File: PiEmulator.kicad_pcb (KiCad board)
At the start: 2 copper layers, 15 parts, among them J3 USB_C_Receptacle_USB2.0, U1 ADA3708, U3 BQ24090DGQ

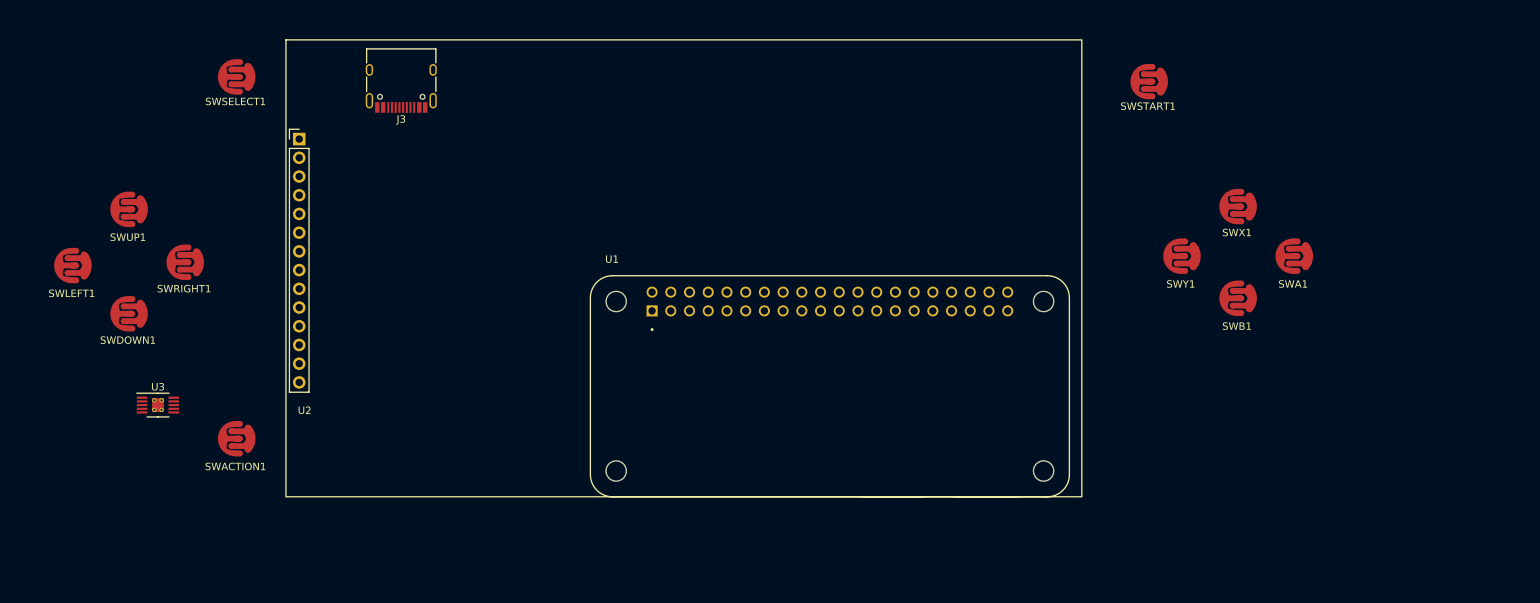
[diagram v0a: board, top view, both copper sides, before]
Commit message: swapped buttons
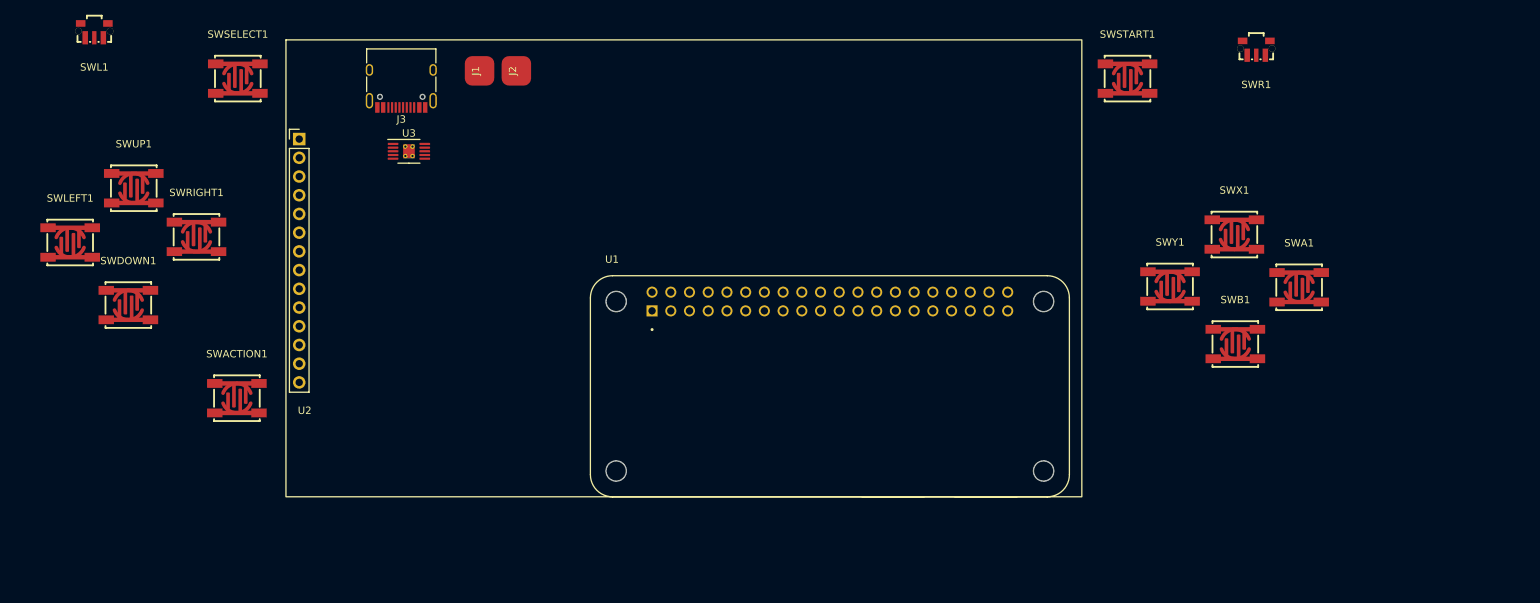
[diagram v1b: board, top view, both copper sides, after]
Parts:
- added J1: Conn_01x01, Connector_Wago:SolderWirePad_4x4mm, F.Cu at (99.8, 61.8)
- added J2: Conn_01x01, Connector_Wire:Solder_Pad_4x4mm, F.Cu at (104.8, 61.8)
- added SWL1: TSA020A3418A, easyeda2kicad:SW-SMD_TSA020XXXXXX, F.Cu at (47.5, 56.4)
- added SWR1: TSA020A3418A, easyeda2kicad:SW-SMD_TSA020XXXXXX, F.Cu at (205.2, 58.8)
- SWA1, SWACTION1, SWB1, SWDOWN1, SWLEFT1, SWRIGHT1, SWSELECT1, SWSTART1, SWUP1, SWX1, SWY1: footprint Button_Switch_SMD:PCB-Button -> easyeda2kicad:SW-SMD_4P-L6.2-W6.2-P4.00-LS7.0
- moved U3 48.4 mm to (90.2, 72.8)
- moved SWACTION1 8.03 mm to (66.8, 106.3)
- moved SWRIGHT1 6.22 mm to (61.4, 84.4)
- moved SWLEFT1 5.67 mm to (44.2, 85.1)
- moved SWUP1 5.47 mm to (52.9, 77.8)
- moved SWSTART1 4.06 mm to (187.7, 62.9)
- moved SWDOWN1 3.72 mm to (52.1, 93.6)
- moved SWB1 3.68 mm to (202.3, 98.9)
- moved SWSELECT1 2.33 mm to (67.0, 62.9)
- moved SWY1 2.15 mm to (193.5, 91.1)
- moved SWA1 1.87 mm to (211.0, 91.2)
- moved SWX1 1.31 mm to (202.2, 84.1)
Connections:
- U3 pad 10: unconnected-(U3-OUT-Pad10) -> Net-(J1-Pin_1)
- U3 pad 5: unconnected-(U3-~{PG}-Pad5) -> Net-(D1-K)
- U3 pad 8: unconnected-(U3-~{CHG}-Pad8) -> Net-(D2-K)
- U3 pad 9: unconnected-(U3-TS-Pad9) -> Net-(U3-TS)

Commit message: routed
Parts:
- added D1: BLUE, LED_SMD:LED_0402_1005Metric, F.Cu at (181.9, 73.5)
- added D2: RED, LED_SMD:LED_0402_1005Metric, F.Cu at (181.9, 75.4)
- added R1: 540, Resistor_SMD:R_0603_1608Metric, B.Cu at (91.2, 70.5)
- added R2: 2K, Resistor_SMD:R_0603_1608Metric, B.Cu at (91.8, 73.2)
- added R3: 1K5, Resistor_SMD:R_0402_1005Metric, F.Cu at (184.0, 73.5)
- added R4: 1K5, Resistor_SMD:R_0402_1005Metric, F.Cu at (184.0, 75.4)
- added R5: 10K, Resistor_SMD:R_0402_1005Metric, B.Cu at (80.9, 72.5)
- J1, J2, J3, U3: moved to B.Cu
- moved J1 11.1 mm to (105.4, 71.4)
- moved J2 10.5 mm to (100.1, 71.2)
- moved SWACTION1 7.15 mm to (62.0, 111.5)
- moved SWX1 7.09 mm to (201.6, 77.0)
- moved SWL1 5.52 mm to (47.3, 61.9)
- moved SWRIGHT1 4.94 mm to (59.6, 89.0)
- moved U3 4.83 mm to (85.5, 71.6), turned to 180 degrees
- moved SWY1 4.39 mm to (189.6, 89.0)
- moved SWR1 4.31 mm to (202.3, 62.0)
- moved SWUP1 4.23 mm to (52.6, 82.0)
- moved SWLEFT1 4.11 mm to (45.6, 89.0)
- moved J3 3.58 mm to (85.6, 63.2), turned to 0 degrees
- moved SWA1 3.44 mm to (213.6, 89.0)
- moved SWSELECT1 3.42 mm to (63.7, 63.9)
- moved U1 3.42 mm to (144.0, 105.6)
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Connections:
- J1 pad 1: Net-(J1-Pin_1) -> +BATT
- U1 pad 12: /A -> /X
- U1 pad 13: unconnected-(U1-GPIO27_GEN2-Pad13) -> /Right
- U1 pad 14: unconnected-(U1-GND_4-Pad14) -> GND
- U1 pad 2: unconnected-(U1-5V_1-Pad2) -> +BATT
- U1 pad 20: unconnected-(U1-GND_5-Pad20) -> GND
- U1 pad 25: unconnected-(U1-GND_2-Pad25) -> GND
- U1 pad 29: /Right -> /Left
- U1 pad 3: /RB -> /Action
- U1 pad 30: /B -> GND
- U1 pad 31: /Left -> /Down
- U1 pad 32: /X -> /A
- U1 pad 33: /Down -> /Up
- U1 pad 34: unconnected-(U1-GND_7-Pad34) -> GND
- U1 pad 35: /Up -> /B
- U1 pad 39: unconnected-(U1-GND_3-Pad39) -> GND
- U1 pad 4: +5V -> +BATT
- U1 pad 40: /Action -> /RB
- U1 pad 9: unconnected-(U1-GND_1-Pad9) -> GND
- U2 pad 1: +5V -> +BATT
- U2 pad 8: +5V -> +BATT
- U3 pad 10: Net-(J1-Pin_1) -> +BATT
- U3 pad 7: unconnected-(U3-ISET2-Pad7) -> GND
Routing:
- net +BATT: track 0.00 -> 188.5 mm, vias 0 -> 1
- net /Up: track 0.00 -> 163.7 mm
- net /Left: track 0.00 -> 123.7 mm
- net /Down: track 0.00 -> 115.5 mm
- net Net-(D2-K): track 0.00 -> 115.3 mm, vias 0 -> 1
- net /Select: track 0.00 -> 110.1 mm, vias 0 -> 1
- net Net-(D1-K): track 0.00 -> 106.4 mm, vias 0 -> 1
- net /LB: track 0.00 -> 97.9 mm
- net /Right: track 0.00 -> 91.3 mm
- net /CLK: track 0.00 -> 87.8 mm, vias 0 -> 1
- net /CS: track 0.00 -> 82.3 mm, vias 0 -> 1
- net /MISO: track 0.00 -> 80.4 mm, vias 0 -> 1
- net /RESET: track 0.00 -> 78.7 mm, vias 0 -> 1
- net /MOSI: track 0.00 -> 77.9 mm, vias 0 -> 1
- net /Action: track 0.00 -> 73.0 mm, vias 0 -> 1
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- added copper zone on B.Cu, net GND
- added copper zone on F.Cu, net GND
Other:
- board outline added: 180 x 60 mm

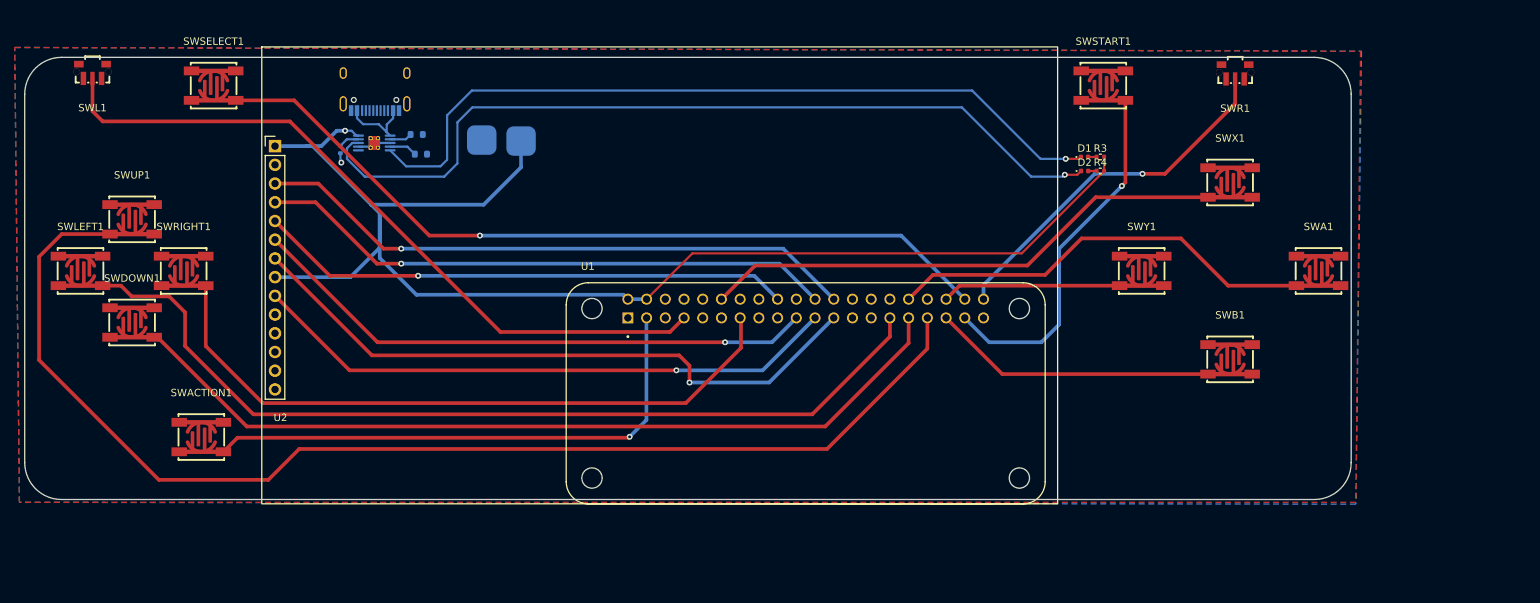
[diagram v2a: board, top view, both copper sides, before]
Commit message: silkscreen + minor fixes
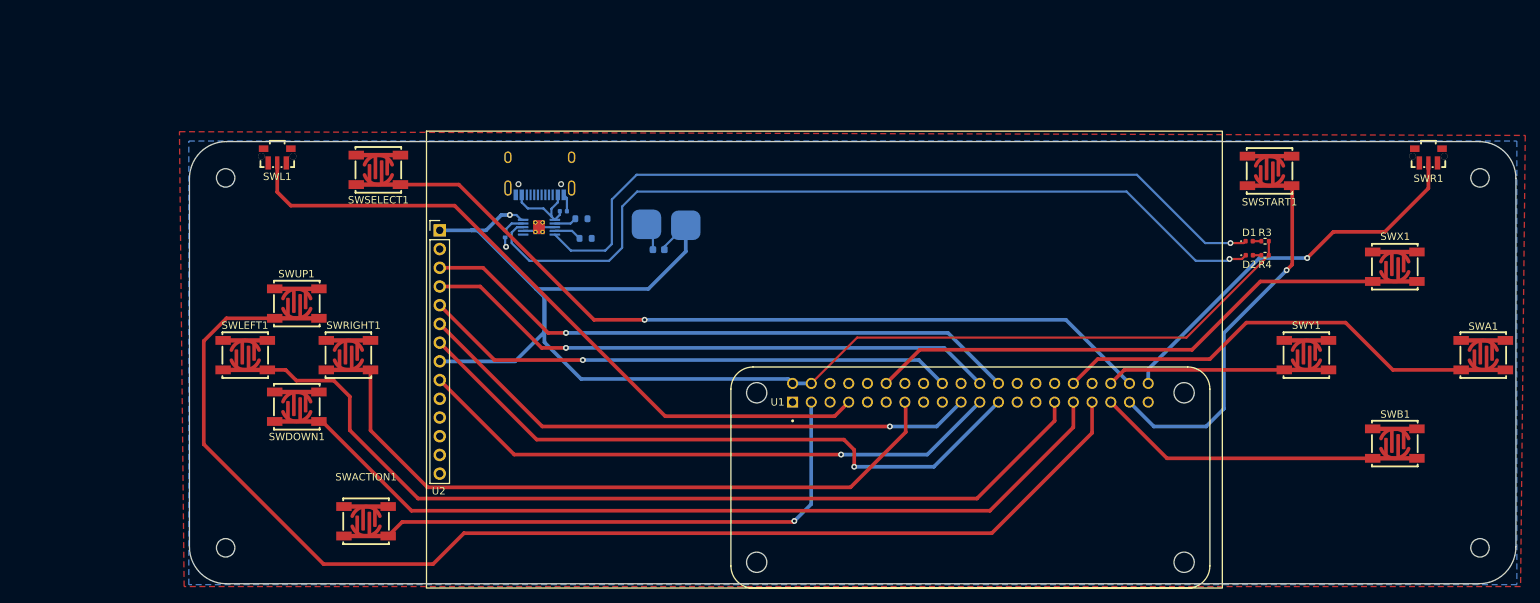
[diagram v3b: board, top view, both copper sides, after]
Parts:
- added C1: 1uF, Capacitor_SMD:C_0402_1005Metric, B.Cu at (111.2, 80.9)
- added C2: 4.7uF, Capacitor_SMD:C_0603_1608Metric, B.Cu at (124.1, 86.1)
- added H1: MountingHole, MountingHole:MountingHole_2.5mm, F.Cu at (65.3, 76.4)
- added H2: MountingHole, MountingHole:MountingHole_2.5mm, F.Cu at (65.3, 126.6)
- added H3: MountingHole, MountingHole:MountingHole_2.5mm, F.Cu at (235.5, 126.6)
- added H4: MountingHole, MountingHole:MountingHole_2.5mm, F.Cu at (235.5, 76.4)
- moved SWR1 28.6 mm to (228.5, 73.4)
- moved SWL1 27.6 mm to (72.3, 73.4)
- moved SWSTART1 25.4 mm to (207.0, 75.4)
- moved J1 25.1 mm to (127.8, 82.8)
- moved J2 25.1 mm to (122.4, 82.7)
- moved R1 25.1 mm to (113.6, 81.9)
- moved SWA1 25.1 mm to (236.0, 100.4)
- moved SWACTION1 25.1 mm to (84.4, 123.0)
- moved SWB1 25.1 mm to (224.0, 112.4)
- moved SWDOWN1 25.1 mm to (75.0, 107.4)
- moved SWLEFT1 25.1 mm to (68.0, 100.4)
- moved SWRIGHT1 25.1 mm to (82.0, 100.4)
- moved SWUP1 25.1 mm to (75.0, 93.4)
- moved SWX1 25.1 mm to (224.0, 88.4)
- moved SWY1 25.1 mm to (212.0, 100.4)
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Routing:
- net GND: track 5.83 -> 12.0 mm
- net +BATT: track 188.5 -> 193.0 mm
- net /RB: track 49.6 -> 53.6 mm
- net /LB: track 97.9 -> 94.9 mm
- net VBUS: track 9.79 -> 11.2 mm

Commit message: added boost convertor
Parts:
- added C3: 22uF, Capacitor_SMD:C_0805_2012Metric, B.Cu at (131.2, 87.9)
- added C4: 10nF, Capacitor_SMD:C_0402_1005Metric, B.Cu at (144.7, 80.6)
- added C5: 22uF, Capacitor_SMD:C_0805_2012Metric, B.Cu at (124.0, 85.5)
- added C6: 22uF, Capacitor_SMD:C_0805_2012Metric, B.Cu at (121.8, 85.5)
- added C7: 22uF, Capacitor_SMD:C_0805_2012Metric, B.Cu at (124.0, 81.9)
- added L1: 1uH, Inductor_SMD:L_0603_1608Metric, B.Cu at (127.4, 88.0)
- added R10: 5.6K, Resistor_SMD:R_0603_1608Metric, B.Cu at (132.4, 83.4)
- added R11: 0.2K, Resistor_SMD:R_0603_1608Metric, B.Cu at (133.1, 81.2)
- added R6: 402K, Resistor_SMD:R_0603_1608Metric, B.Cu at (137.9, 76.7)
- added R7: 100K, Resistor_SMD:R_0603_1608Metric, B.Cu at (137.9, 79.2)
- added R8: 1.0Meg, Resistor_SMD:R_0603_1608Metric, B.Cu at (137.9, 81.7)
- added R9: 10K, Resistor_SMD:R_0402_1005Metric, B.Cu at (133.0, 85.5)
- added U4: TPS61230DRCR, easyeda2kicad:VSON-10_L3.0-W3.0-P0.50-TL-EP_TPS61230DRCR, B.Cu at (127.3, 84.7)
- moved J1 25.8 mm to (102.9, 76.1)
- moved J2 25.8 mm to (97.5, 76.0)
- moved C2 24.9 mm to (100.1, 79.5)
- moved J3 4.49 mm to (112.4, 74.2)
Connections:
- U1 pad 2: +BATT -> +5V
- U1 pad 4: +BATT -> +5V
- U2 pad 1: +BATT -> +5V
- U2 pad 8: +BATT -> +5V
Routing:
- net +5V: track 0.00 -> 100.2 mm, vias 0 -> 2
- net +BATT: track 193.0 -> 105.2 mm
- net Net-(D1-K): track 106.4 -> 99.4 mm
- net Net-(D2-K): track 115.3 -> 108.5 mm
- net Net-(U4-HYS): track 0.00 -> 6.14 mm
- net Net-(U4-EN): track 0.00 -> 5.10 mm
- net Net-(L1-Pad1): track 0.00 -> 3.16 mm
- net GND: track 12.0 -> 10.1 mm
- net VBUS: track 11.2 -> 10.7 mm

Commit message: bost routing + cleanup
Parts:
- moved C4 14.2 mm to (130.5, 80.8)
- moved R8 11.9 mm to (126.3, 79.1), turned to 90 degrees
- moved R6 8.02 mm to (129.9, 77.5), turned to -90 degrees
- moved R7 6.53 mm to (131.6, 77.5), turned to 90 degrees
- moved C7 2.55 mm to (121.8, 80.5)
- moved R10 2.25 mm to (133.9, 81.8)
- moved R11 2.25 mm to (134.6, 79.5)
- moved R9 2.25 mm to (134.5, 83.8)
- moved U4 1.83 mm to (128.1, 83.0)
- moved C3 1.47 mm to (132.4, 87.0)
- moved C5 1.46 mm to (124.0, 84.0)
- moved C6 1.46 mm to (121.8, 84.0)
- moved L1 1.01 mm to (128.0, 87.2)
- moved R1 0.51 mm to (113.7, 82.4)
- moved C1 0.13 mm to (111.1, 80.8)
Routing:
- net +BATT: track 105.2 -> 141.2 mm, vias 1 -> 2
- net +5V: track 100.2 -> 115.3 mm
- net Net-(U4-FB): track 0.00 -> 7.12 mm
- net /Start: track 49.6 -> 55.9 mm
- net Net-(U4-PG): track 0.00 -> 2.28 mm
- net Net-(U4-SS): track 0.00 -> 1.98 mm
- net Net-(D2-K): track 108.5 -> 107.3 mm
- net /RB: track 53.6 -> 52.4 mm
- net Net-(D1-K): track 99.4 -> 98.4 mm
- net Net-(U4-EN): track 5.10 -> 6.00 mm
- net Net-(L1-Pad1): track 3.16 -> 3.99 mm
- net Net-(U4-HYS): track 6.14 -> 6.74 mm
- net GND: vias 1 -> 19
